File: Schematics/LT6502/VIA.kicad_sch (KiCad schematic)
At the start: 6 parts, among them IC3 W65C22S6TQG-14, J11 Conn_02x04_Odd_Even, J12 Conn_02x06_Odd_Even, J13 Conn_02x06_Odd_Even

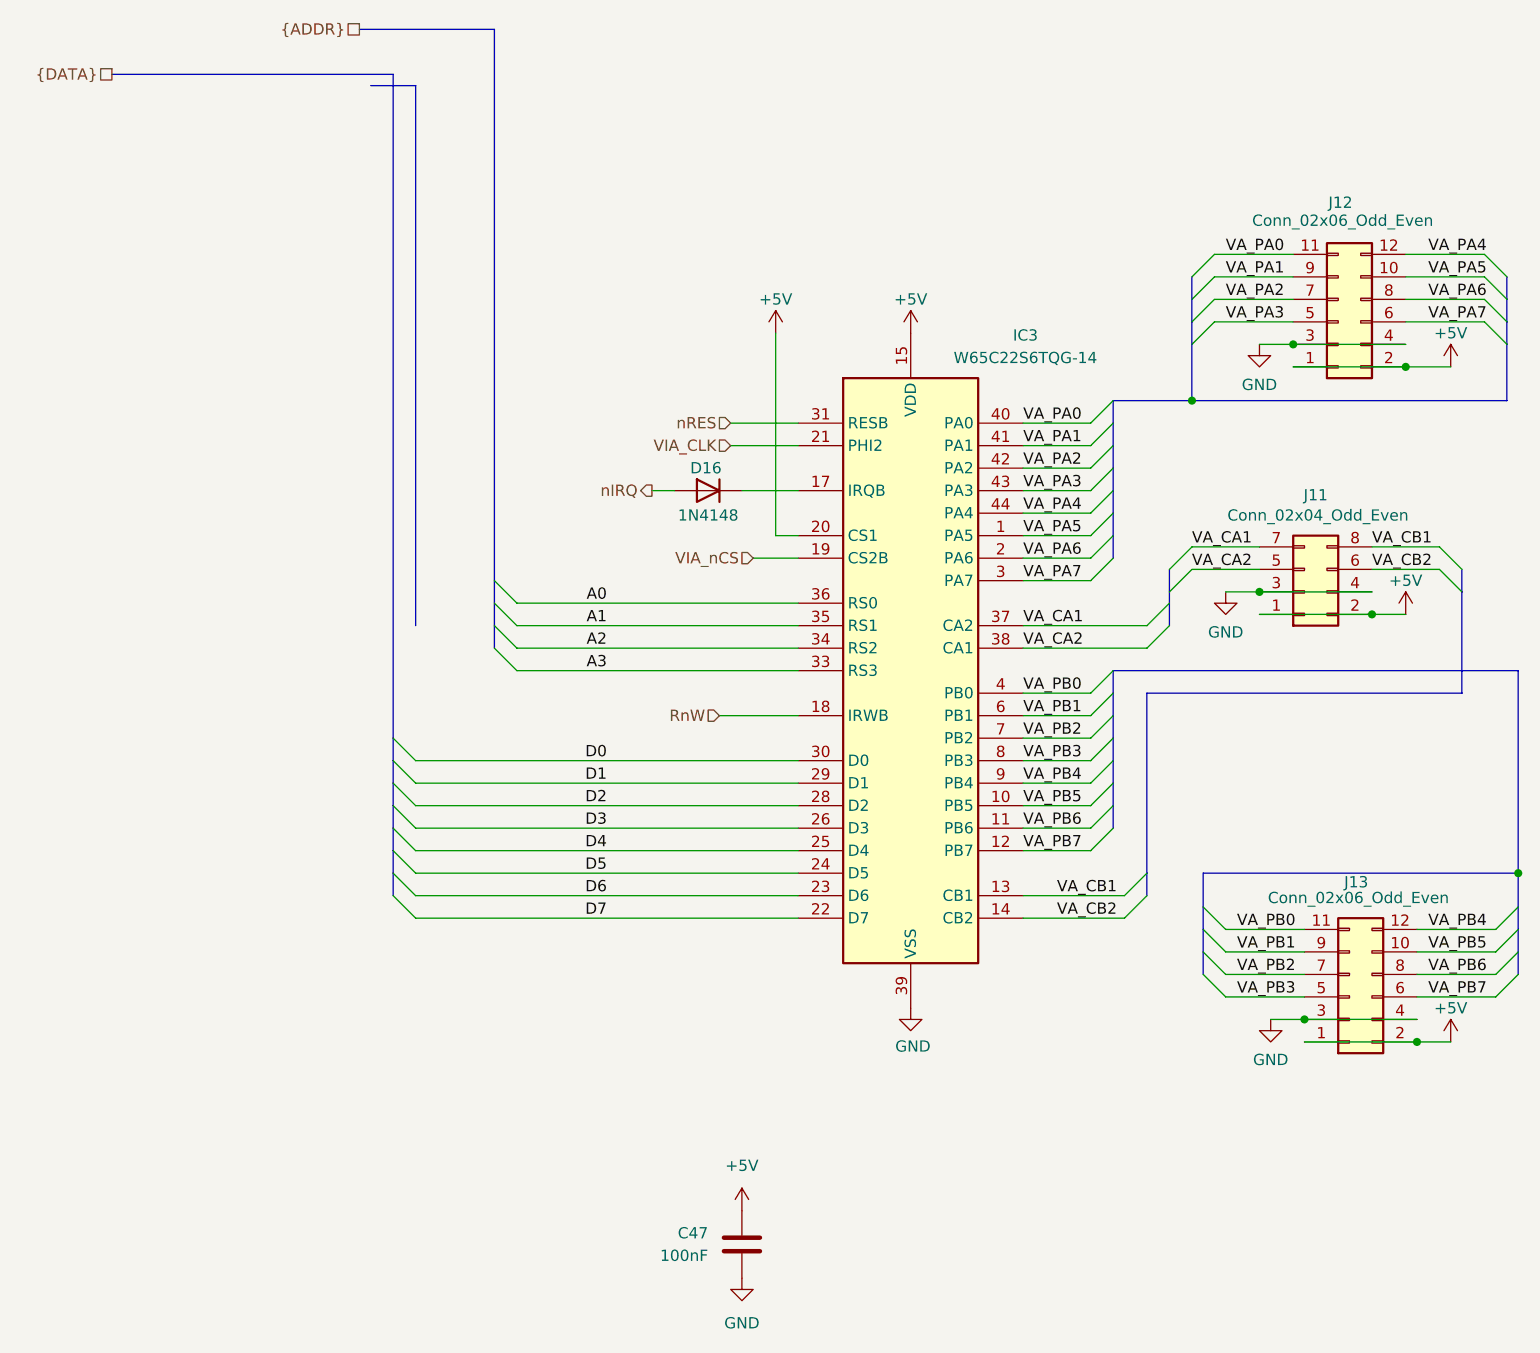
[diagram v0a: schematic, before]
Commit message: Updated main board and started keybed
main board a bit wider due to keybed width
created keybed, begun routing
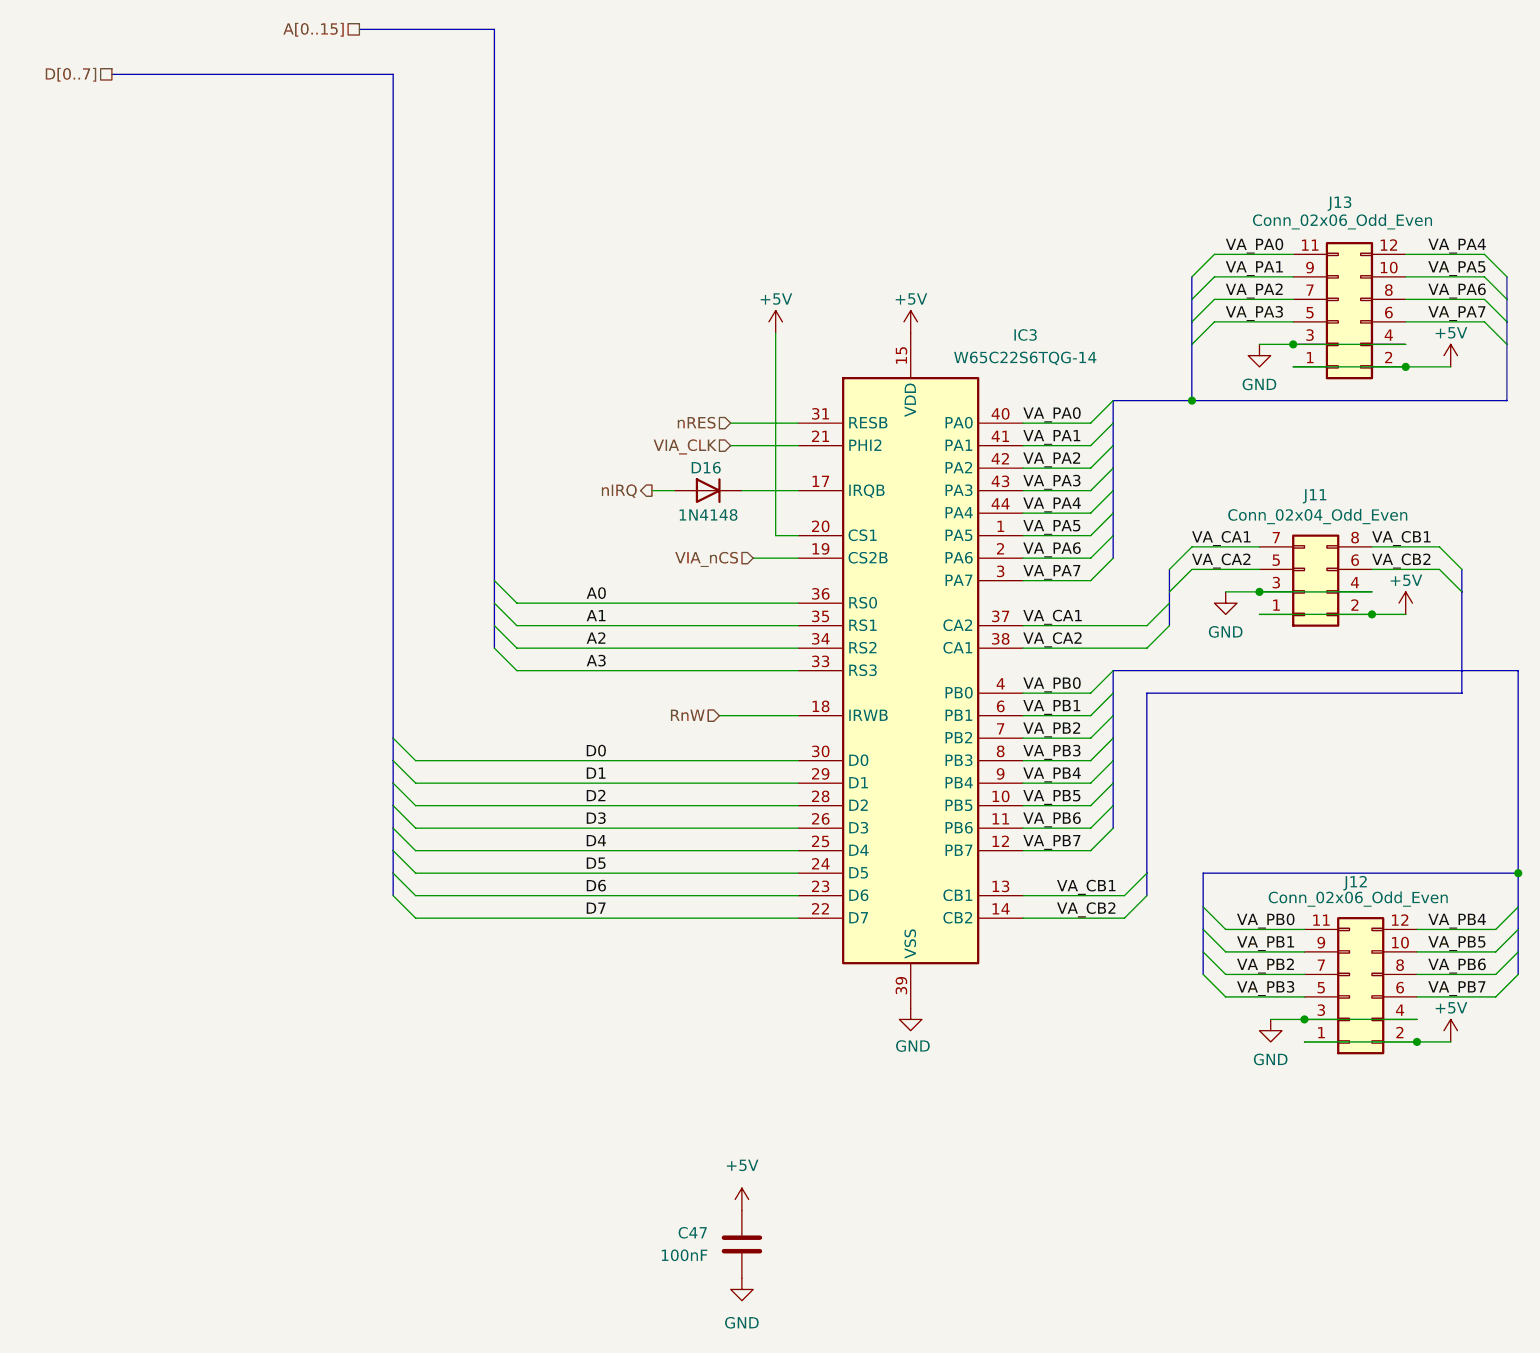
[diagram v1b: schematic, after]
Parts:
- renumbered J13 to J12, J12 to J13

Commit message: Updated BoMs ordered PCBs
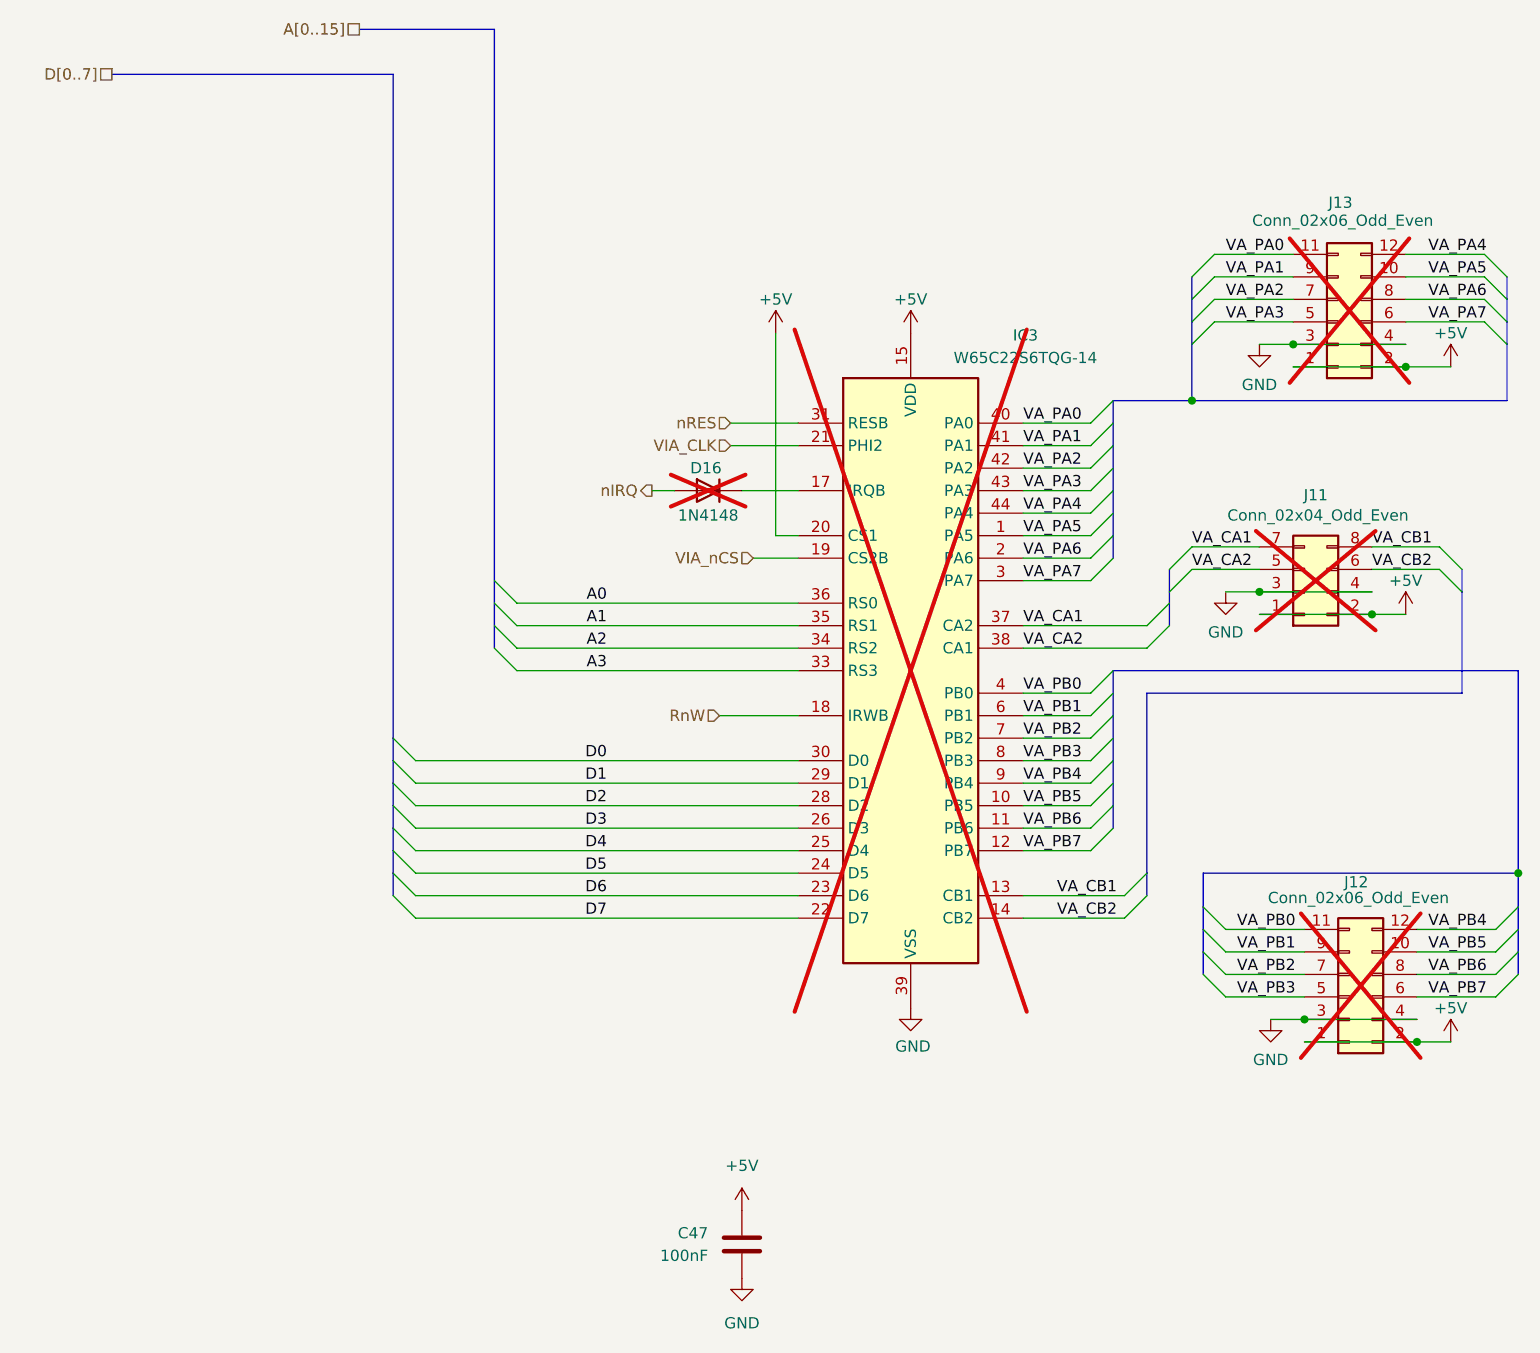
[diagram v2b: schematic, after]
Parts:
- C47: LCSC C49678 -> C113803
- D16, IC3, J11, J12, J13: LCSC (none) -> DNF; now not fitted
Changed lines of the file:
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@@
 		(in_bom yes)
 		(on_board yes)
-		(dnp no)
+		(dnp yes)
 		(property "Reference" "J12"
 			(at 198.882 130.556 0)
@@
 		)
 		(property "Description" "Generic connector, double row, 02x06, odd/even pin numbering scheme (row 1 odd numbers, row 2 even numbers), script generated (kicad-library-utils/schlib/autogen/connector/)"
+			(at 198.12 143.51 0)
+			(effects
+				(font
+					(size 1.27 1.27)
+				)
+				(hide yes)
+			)
+		)
+		(property "LCSC" "DNF"
 			(at 198.12 143.51 0)
 			(effects
@@
 		(in_bom yes)
 		(on_board yes)
-		(dnp no)
+		(dnp yes)
 		(property "Reference" "J11"
 			(at 194.31 86.868 0)
@@
 		)
 		(property "Description" "Generic connector, double row, 02x04, odd/even pin numbering scheme (row 1 odd numbers, row 2 even numbers), script generated (kicad-library-utils/schlib/autogen/connector/)"
+			(at 193.04 97.79 0)
+			(effects
+				(font
+					(size 1.27 1.27)
+				)
+				(hide yes)
+			)
+		)
+		(property "LCSC" "DNF"
 			(at 193.04 97.79 0)
 			(effects
@@
 		(in_bom yes)
 		(on_board yes)
-		(dnp no)
+		(dnp yes)
 		(fields_autoplaced yes)
 		(property "Reference" "IC3"
@@
 			)
 		)
+		(property "LCSC" "DNF"
+			(at 148.59 106.68 0)
+			(effects
+				(font
+					(size 1.27 1.27)
+				)
+				(hide yes)
+			)
+		)
 		(pin "1"
 		)
@@
 		(in_bom yes)
 		(on_board yes)
-		(dnp no)
+		(dnp yes)
 		(property "Reference" "D16"
 			(at 125.476 83.82 0)
@@
 		)
 		(property "Sim.Pins" "1=K 2=A"
+			(at 125.73 86.36 0)
+			(effects
+				(font
+					(size 1.27 1.27)
+				)
+				(hide yes)
+			)
+		)
+		(property "LCSC" "DNF"
 			(at 125.73 86.36 0)
 			(effects
@@
 		(in_bom yes)
 		(on_board yes)
-		(dnp no)
+		(dnp yes)
 		(property "Reference" "J13"
 			(at 197.104 53.848 0)
@@
 		)
 		(property "Description" "Generic connector, double row, 02x06, odd/even pin numbering scheme (row 1 odd numbers, row 2 even numbers), script generated (kicad-library-utils/schlib/autogen/connector/)"
+			(at 196.85 67.31 0)
+			(effects
+				(font
+					(size 1.27 1.27)
+				)
+				(hide yes)
+			)
+		)
+		(property "LCSC" "DNF"
 			(at 196.85 67.31 0)
 			(effects
@@
 			)
 		)
-		(property "LCSC" "C49678"
+		(property "LCSC" "C113803"
 			(at 129.54 171.45 0)
 			(effects

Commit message: Auto stash before merge of "main" and "origin/main"
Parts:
- D16, IC3, J11, J12, J13: now fitted
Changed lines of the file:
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@@
 		(in_bom yes)
 		(on_board yes)
-		(dnp yes)
+		(dnp no)
 		(property "Reference" "J12"
 			(at 198.882 130.556 0)
@@
 		(in_bom yes)
 		(on_board yes)
-		(dnp yes)
+		(dnp no)
 		(property "Reference" "J11"
 			(at 194.31 86.868 0)
@@
 		(in_bom yes)
 		(on_board yes)
-		(dnp yes)
+		(dnp no)
 		(fields_autoplaced yes)
 		(property "Reference" "IC3"
@@
 		(in_bom yes)
 		(on_board yes)
-		(dnp yes)
+		(dnp no)
 		(property "Reference" "D16"
 			(at 125.476 83.82 0)
@@
 		(in_bom yes)
 		(on_board yes)
-		(dnp yes)
+		(dnp no)
 		(property "Reference" "J13"
 			(at 197.104 53.848 0)
